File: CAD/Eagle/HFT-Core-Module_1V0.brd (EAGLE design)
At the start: 96.5 x 96.5 mm, 333 parts, among them Q0521 ABS07-32.768KHZ, Q0811 ABM03B-32.000MHZ, Q0911 ABM3B-16MHZ-10-R50-1-U, T1101 MMBT2222, T1102 MMBT2222, T1103 MMBT2222, U0111 STM32L4Z_144PIN_SMPS, U0431 PAM2305AAB120, U0601 LM4120IM5-3.0, U0611 MAX5217, U0631 CFPT-141-20MHZ, U0641 OPA354, U0701 Si5338, U0801 SX1276, U0901 AX5243, U1001 MCP3911A0-E-SS, U1011 MAX5136AGTG+, U1021 OPA354, U1031 OPA354, U1041 OPA354, U1101 NHD-C0220BIZ_2X20CHARS, U1201 MPU-9250, U1211 MS5607-02BA03, U1221 SHT31-DIS, U1301 SOLARPANEL_3V3_5MA1_25MM_X_20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, U1302 SPV1040T, U1401 TS5A23166, U1501 PAM2305AAB330, U1601 TS5A23166, U1701 TS5A23166, U1801 TS5A23166, X1161 TTE_EN11-HSM, X2001 SMA_SMT_AMPHENOL-901-143, X2011 SMA_SMT_AMPHENOL-901-143, X2101 CUI SJ1-3535NS, X2111 CUI SJ1-3535NS, X2211 2X20/90_1MM27_HARWIN_M50-3202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, X2212 2X20/90_1MM27_HARWIN_M50-3202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, X2221 2X20/90_1MM27_HARWIN_M50-3202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, X2222 2X20/90_1MM27_HARWIN_M50-3202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, X2231 2X20/90_1MM27_HARWIN_M50-3202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, X2232 2X20/90_1MM27_HARWIN_M50-3202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

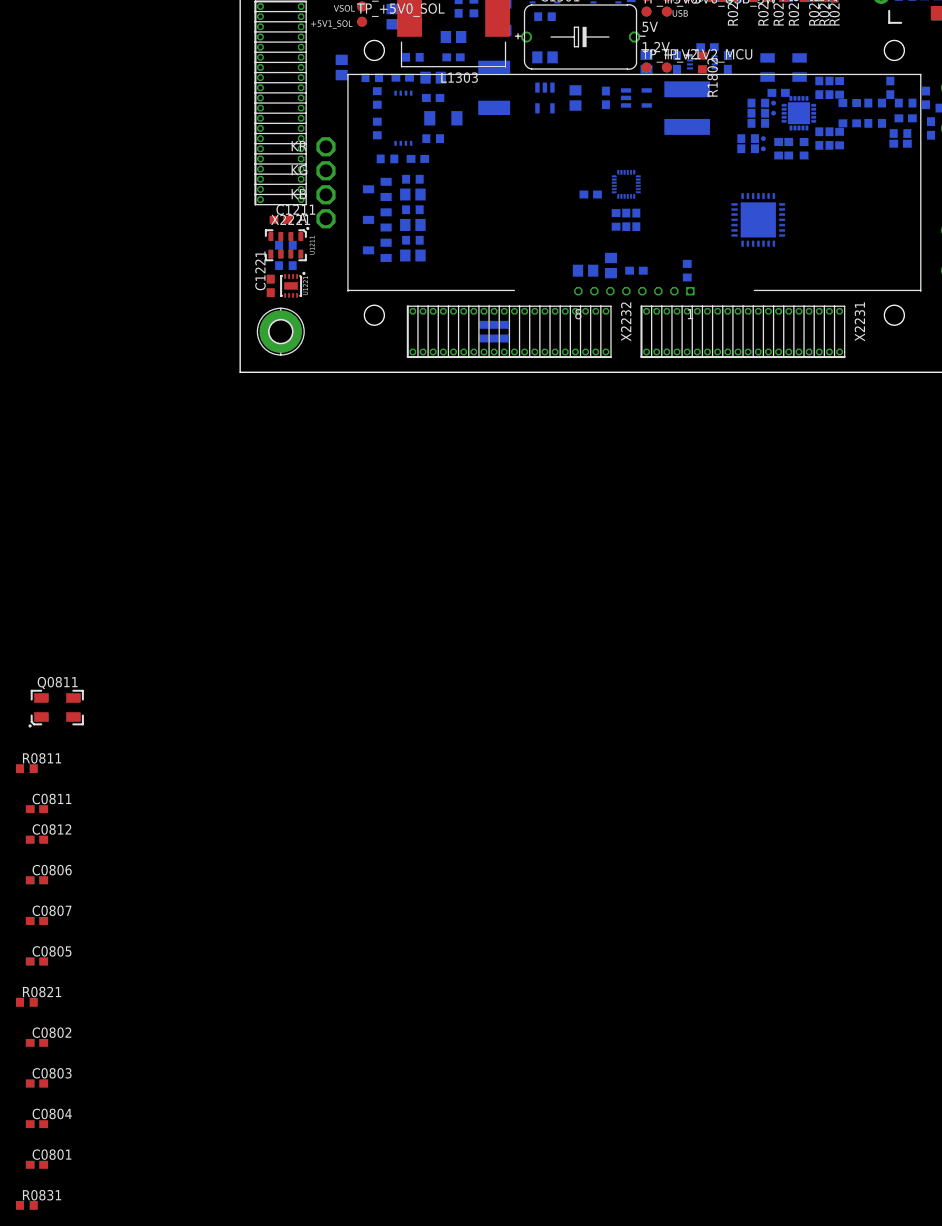
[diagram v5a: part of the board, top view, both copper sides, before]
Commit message: HW_1V0_trySX - some of the SX chip components placed
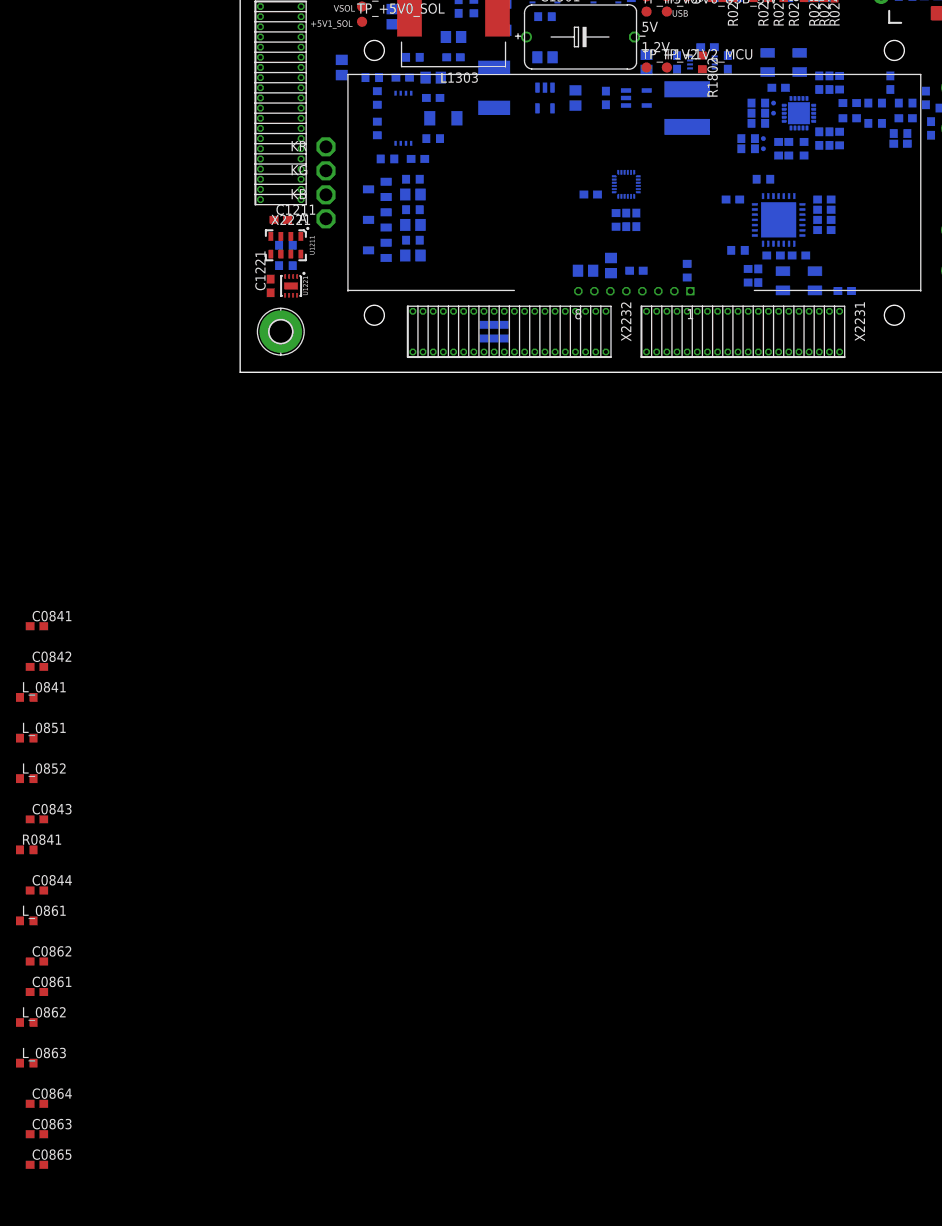
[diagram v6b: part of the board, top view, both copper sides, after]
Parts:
- added C0841, C0842, C0843, C0844, C0861, C0862, C0863, C0864, C0865: (no value), rcl:C0603
- added L_0841, L_0851, L_0852, L_0861, L_0862, L_0863: (no value), rcl:R0603
- added R0841: 0R, rcl:R0603
- moved R0831 157.9 mm to (65.4, 24.1), flipped to the bottom, turned to 180 degrees
- moved C0801 155.7 mm to (73.0, 21.6), flipped to the bottom, turned to 180 degrees
- moved C0803 145.1 mm to (73.0, 17.8), flipped to the bottom
- moved C0804 144.7 mm to (61.6, 21.6), flipped to the bottom, turned to 180 degrees
- moved C0802 143.3 mm to (73.0, 20.3), flipped to the bottom
- moved C0805 135.2 mm to (73.0, 19.1), flipped to the bottom
- moved R0821 129.4 mm to (62.2, 15.2), flipped to the bottom, turned to 180 degrees
- moved C0807 124.1 mm to (66.7, 14.6), flipped to the bottom, turned to 180 degrees
- moved C0806 123.2 mm to (69.8, 14.6), flipped to the bottom
- moved C0812 122.1 mm to (75.6, 10.2), flipped to the bottom
- moved C0811 112.1 mm to (64.8, 12.1), flipped to the bottom, turned to 270 degrees
- moved R0811 109.2 mm to (63.5, 12.1), flipped to the bottom, turned to 270 degrees
- moved Q0811 107.0 mm to (69.8, 11.4), flipped to the bottom, turned to 180 degrees
- moved U0801 2.54 mm to (67.3, 19.1), turned to 90 degrees
- moved C0901 0.64 mm to (67.3, 35.6)
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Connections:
- net XTB_R renamed SX_XTB_R
- new net N$1: C0844.2
- new net SX_PA_BOOST: L_0851.1, U0801.27
- new net SX_PA_BOOST_2: L_0851.2, L_0852.1
- new net SX_RFI_HF: C0841.1, L_0841.1, U0801.21
- new net SX_RFI_HF_2: C0842.1, C0843.1, L_0841.2
- new net SX_RFI_HF_3: C0843.2, R0841.1
- new net SX_RFI_HF_4: C0844.1, R0841.2
- new net SX_RFO_HF: C0861.1, C0862.1, L_0861.1, U0801.22
- new net SX_RFO_HF_2: C0862.2, L_0862.1
- new net SX_RFO_HF_3: C0863.1, C0864.1, L_0862.2, L_0863.1
- new net SX_RFO_HF_4: C0864.2, C0865.1, L_0863.2
- net GND: now also C0841.2, C0842.2, C0861.2, C0863.2, C0865.2
- net SX_VR_PA: now also L_0852.2, L_0861.2

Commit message: HW_1V0_trySX - RF front end added
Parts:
- removed C0842: (no value), rcl:C0603
- removed L_0851: (no value), rcl:R0603
- removed R0922: 47R, rcl:R0603
- added C0846, C0873, C0975: 47pF, rcl:C0603
- added C0850, C0858, C0872: 0pF, rcl:C0603
- added C0851, C0852: (no value), rcl:C0603
- added C0853, C0871: 4.7pF, rcl:C0603
- added C0856, C0859: 6.8pF, rcl:C0603
- added C0857: 2.7pF, rcl:C0603
- added L0854: 15nH, rcl:R0603
- added L0856, L0858, R0874: 0R, rcl:R0603
- added L0857: 12nH, rcl:R0603
- added L0871: 18nH, rcl:R0603
- added R0801: 100R, rcl:R0603
- added R0802, R0803, R0804, R0805, R0806, R0807: 47R, rcl:R0603
- C0841: value (none) -> 0pF
- C0843: value (none) -> 3.3pF
- C0844: value (none) -> 47pF
- C0861: value (none) -> 1.5pF
- C0862: value (none) -> 33pF
- C0863: value (none) -> 4.7pF
- C0864: value (none) -> 1.2pF
- C0865: value (none) -> 1.8pF
- L0842, L0862: value (none) -> 10nH
- L0851: value (none) -> 68nH
- L0861: value (none) -> 33nH
- L0864: value (none) -> 6.2nH
- moved C0843 19.1 mm to (-25.4, -36.8)
- moved C0844 8.89 mm to (-25.4, -55.9)
- renumbered L_0841 to L0842, L_0852 to L0851, L_0861 to L0861, L_0862 to L0862, L_0863 to L0864, R0841 to R0845
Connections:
- removed net AX1_SYSCLK_R: R0922.2
- removed net N$1: C0844.2
- removed net SX_PA_BOOST: L_0851.1, U0801.27
- removed net SX_PA_BOOST_2: L0851.1, L_0851.2
- new net SX_DIO0: R0802.1, U0801.8
- new net SX_DIO0_2: R0802.2
- new net SX_DIO1: R0803.1, U0801.9
- new net SX_DIO1_2: R0803.2
- new net SX_DIO2: R0804.1, U0801.10
- new net SX_DIO2_2: R0804.2
- new net SX_DIO3: R0805.1, U0801.11
- new net SX_DIO3_2: R0805.2
- new net SX_DIO4: R0806.1, U0801.12
- new net SX_DIO4_2: R0806.2
- new net SX_DIO5: R0807.1, U0801.13
- new net SX_DIO5_2: R0807.2
- new net SX_RFI_HF_5: C0846.2
- new net SX_RFI_LF: C0871.1, L0871.1, U0801.1
- new net SX_RFI_LF_2: C0871.2, C0872.2, C0873.1
- new net SX_RFI_LF_3: C0873.2, R0874.1
- new net SX_RFI_LF_4: C0975.1, R0874.2
- new net SX_RFI_LF_5: C0975.2
- new net SX_RFO_LF: C0853.1, L0851.1, L0854.1, U0801.28
- new net SX_RFO_LF_2: L0854.2, L0856.1
- new net SX_RFO_LF_3: C0856.1, C0857.1, L0856.2, L0857.1
- new net SX_RFO_LF_4: C0857.2, C0858.1, C0859.1, L0857.2, L0858.1
- new net SX_RFO_LF_5: C0850.1, C0858.2, L0858.2
- new net SX_RXTX: R0801.1, U0801.20
- new net SX_RXTX_2: R0801.2
- net AX1_SYSCLK: no longer R0922.1
- net GND: now also C0843.2, C0850.2, C0851.2, C0852.2, C0853.2, C0856.2, C0859.2, C0872.1, L0871.2; no longer C0842.2
- net SX_RFI_HF_2: now also C0844.1; no longer C0842.1
- net SX_RFI_HF_3: now also C0844.2; no longer C0843.2
- net SX_RFI_HF_4: now also C0846.1; no longer C0844.1
- net SX_VR_PA: now also C0851.1, C0852.1

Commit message: HW_1V0_trySX - renaming of nets to match with the MCU
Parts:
- R0723: value none -> 47R
- R0804, R0805, R0806, R0807: value 47R -> NC
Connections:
- net AX1_16MHZ renamed AX_16MHZ
- net AX1_SYSCLK renamed AX_SYSCLK
- net MCU_20MHZ_EN renamed MCU_OUT_20MHZ_EN
- net MCU_AX1_GPO1 renamed AX_GPIO1
- net MCU_AX1_IRQ renamed AX_IRQ
- net MCU_HICUR_EN renamed MCU_OUT_HICUR_EN
- net MCU_LCD_!RST renamed MCU_OUT_LCD_NRST
- net MCU_SPI3_AUDIO_ADC_!RESET renamed MCU_OUT_AUDIO_ADC_NRESET
- net MCU_SPI3_AUDIO_ADC_SEL renamed MCU_OUT_AUDIO_ADC_SEL
- net MCU_SPI3_AUDIO_DAC_SEL renamed MCU_OUT_AUDIO_DAC_SEL
- net MCU_SPI3_AX1_SEL renamed MCU_OUT_AX_SEL
- net MCU_SPI3_SX_SEL renamed MCU_OUT_SX_SEL
- net MCU_VDD12_EN renamed MCU_OUT_VDD12_EN
- net MCU_VUSB_EN renamed MCU_OUT_VUSB_EN
- net PC14_OSC32_IN renamed PC14_MCU_OSC32_IN
- net PC15_OSC32_OUT renamed PC15_MCU_OSC32_OUT
- net SX_!RESET_R renamed SX_NRESET
- removed net AX1_ANT: C_AX1_A3.1, C_AX1_F2.2, L_AX1_F1.2, X2001.1
- removed net AX2_ANT: X2011.1
- removed net CLK3B: R0723.1
- removed net PH0_OSC_IN: R0724.1, U0111.23, U1001.12
- removed net SX_!RESET: R0821.1
- removed net SX_DIO0_2: R0802.2
- removed net SX_DIO1_2: R0803.2
- new net CH1_ANT: X2001.1
- new net CH2_ANT: C_AX1_A3.1, C_AX1_F2.2, L_AX1_F1.2, X2011.1
- new net PH0: R0724.1, U0111.23
- new net SI5338_CLK3B_2: R0723.1, U1001.12
- net PD8: now also R0821.1
- net PG2: now also R0802.2
- net PG3: now also R0803.2
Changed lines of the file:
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@@
 <element name="R0731" library="rcl" package="R0603" value="47R" x="73.025" y="85.09"/>
 <element name="R0724" library="rcl" package="R0603" value="47R" x="73.025" y="83.82" rot="R180"/>
-<element name="R0723" library="rcl" package="R0603" value="none" x="73.025" y="82.55" rot="R180"/>
+<element name="R0723" library="rcl" package="R0603" value="47R" x="73.025" y="82.55" rot="R180"/>
 <element name="R0743" library="rcl" package="R0603" value="47R" x="64.135" y="83.82" rot="R180"/>
 <element name="R0744" library="rcl" package="R0603" value="47R" x="64.135" y="82.55" rot="R180"/>
@@
 <element name="R0801" library="rcl" package="R0603" value="100R" x="-26.67" y="-189.23"/>
 <element name="R0803" library="rcl" package="R0603" value="47R" x="-26.67" y="-194.31"/>
-<element name="R0805" library="rcl" package="R0603" value="47R" x="-26.67" y="-199.39"/>
-<element name="R0807" library="rcl" package="R0603" value="47R" x="-26.67" y="-204.47"/>
+<element name="R0805" library="rcl" package="R0603" value="NC" x="-26.67" y="-199.39"/>
+<element name="R0807" library="rcl" package="R0603" value="NC" x="-26.67" y="-204.47"/>
 <element name="R0802" library="rcl" package="R0603" value="47R" x="-26.67" y="-209.55"/>
-<element name="R0804" library="rcl" package="R0603" value="47R" x="-26.67" y="-214.63"/>
-<element name="R0806" library="rcl" package="R0603" value="47R" x="-26.67" y="-219.71"/>
+<element name="R0804" library="rcl" package="R0603" value="NC" x="-26.67" y="-214.63"/>
+<element name="R0806" library="rcl" package="R0603" value="NC" x="-26.67" y="-219.71"/>
 </elements>
 <signals>
@@
 <wire x1="45.085" y1="58" x2="46.99" y2="58" width="0" layer="19" extent="1-1"/>
 </signal>
-<signal name="PH0_OSC_IN">
+<signal name="PH0">
 <contactref element="U0111" pad="23"/>
 <contactref element="R0724" pad="1"/>
-<contactref element="U1001" pad="12"/>
-<wire x1="75.505" y1="83.32" x2="73.875" y2="83.82" width="0" layer="19" extent="1-16"/>
 <wire x1="55.415" y1="60.43" x2="73.875" y2="83.82" width="0" layer="19" extent="1-1"/>
 </signal>
-<signal name="PC15_OSC32_OUT">
+<signal name="PC15_MCU_OSC32_OUT">
 <contactref element="U0111" pad="9"/>
 <contactref element="Q0521" pad="1"/>
@@
 <wire x1="49.11" y1="71.12" x2="49.55" y2="68.58" width="0" layer="19" extent="1-1"/>
 </signal>
-<signal name="PC14_OSC32_IN">
+<signal name="PC14_MCU_OSC32_IN">
 <contactref element="U0111" pad="8"/>
 <contactref element="Q0521" pad="2"/>
@@
 <signal name="PG3">
 <contactref element="U0111" pad="88"/>
+<contactref element="R0803" pad="2"/>
+<wire x1="76.665" y1="61.505" x2="-25.82" y2="-194.31" width="0" layer="19" extent="1-1"/>
 </signal>
 <signal name="PG2">
 <contactref element="U0111" pad="87"/>
+<contactref element="R0802" pad="2"/>
+<wire x1="76.665" y1="61.005" x2="-25.82" y2="-209.55" width="0" layer="19" extent="1-1"/>
 </signal>
 <signal name="PD7">
@@
 <signal name="PD8">
 <contactref element="U0111" pad="77"/>
+<contactref element="R0821" pad="1"/>
+<wire x1="61.38" y1="15.24" x2="76.665" y2="56.005" width="0" layer="19" extent="1-16"/>
 </signal>
 <signal name="PC12">
@@
 <wire x1="55.88" y1="46.99" x2="47.27" y2="47.24" width="0" layer="19" extent="1-16"/>
 </signal>
-<signal name="MCU_20MHZ_EN">
+<signal name="MCU_OUT_20MHZ_EN">
 <contactref element="U0601" pad="3"/>
 <contactref element="U1701" pad="3"/>
@@
 <signal name="P$8">
 </signal>
-<signal name="MCU_VUSB_EN">
+<signal name="MCU_OUT_VUSB_EN">
 <contactref element="U1401" pad="3"/>
 <contactref element="U1401" pad="7"/>
@@
 <wire x1="36.55" y1="46.74" x2="39.65" y2="47.24" width="0" layer="19" extent="16-16"/>
 </signal>
-<signal name="MCU_HICUR_EN">
+<signal name="MCU_OUT_HICUR_EN">
 <contactref element="U1601" pad="3"/>
 <contactref element="U1601" pad="7"/>
@@
 <wire x1="64.985" y1="82.55" x2="66.63" y2="82.935" width="0" layer="19" extent="1-1"/>
 </signal>
-<signal name="CLK3B">
+<signal name="SI5338_CLK3B_2">
 <contactref element="R0723" pad="1"/>
+<contactref element="U1001" pad="12"/>
+<wire x1="75.505" y1="83.32" x2="73.875" y2="82.55" width="0" layer="19" extent="1-16"/>
 </signal>
 <signal name="SI5338_IN_CLK1">
@@
 <wire x1="70.485" y1="28.79" x2="70.35" y2="30.535" width="0" layer="19" extent="16-16"/>
 </signal>
-<signal name="AX1_SYSCLK">
+<signal name="AX_SYSCLK">
 <contactref element="U0901" pad="9"/>
 <contactref element="R0921" pad="1"/>
 <wire x1="67.31" y1="28.79" x2="69.35" y2="30.535" width="0" layer="19" extent="16-16"/>
 </signal>
-<signal name="AX1_16MHZ">
+<signal name="AX_16MHZ">
 <contactref element="R0921" pad="2"/>
 <contactref element="R0714" pad="1"/>
 <wire x1="67.31" y1="27.09" x2="69.215" y2="77.89" width="0" layer="19" extent="1-16"/>
 </signal>
-<signal name="MCU_AX1_IRQ">
+<signal name="AX_IRQ">
 <contactref element="U0901" pad="14"/>
 <contactref element="R0951" pad="2"/>
@@
 <wire x1="65.62" y1="31.115" x2="68" y2="31.885" width="0" layer="19" extent="16-16"/>
 </signal>
-<signal name="MCU_AX1_GPO1">
+<signal name="AX_GPIO1">
 <contactref element="R0961" pad="2"/>
 <contactref element="U0901" pad="15"/>
@@
 <wire x1="86.36" y1="31.33" x2="87.415" y2="33.02" width="0" layer="19" extent="16-16"/>
 </signal>
-<signal name="AX1_ANT">
+<signal name="CH2_ANT">
 <contactref element="L_AX1_F1" pad="2"/>
 <contactref element="C_AX1_F2" pad="2"/>
 <contactref element="C_AX1_A3" pad="1"/>
-<contactref element="X2001" pad="1"/>
-<wire x1="89.115" y1="33.02" x2="91.44" y2="33.02" width="0" layer="19" extent="16-16"/>
-<wire x1="91.44" y1="30.695" x2="91.44" y2="33.02" width="0" layer="19" extent="16-16"/>
-<wire x1="85.725" y1="35.14" x2="89.115" y2="33.02" width="0" layer="19" extent="16-16"/>
-</signal>
-<signal name="AX2_ANT">
 <contactref element="X2011" pad="1"/>
+<wire x1="91.44" y1="30.695" x2="89.115" y2="33.02" width="0" layer="19" extent="16-16"/>
+<wire x1="85.725" y1="35.14" x2="89.115" y2="33.02" width="0" layer="19" extent="16-16"/>
+<wire x1="91.44" y1="15.24" x2="91.44" y2="30.695" width="0" layer="19" extent="16-16"/>
 </signal>
 <signal name="LCD_C1+">
@@
 <wire x1="67.31" y1="22.025" x2="68" y2="32.385" width="0" layer="19" extent="16-16"/>
 </signal>
-<signal name="MCU_SPI3_AX1_SEL">
+<signal name="MCU_OUT_AX_SEL">
 <contactref element="R0253" pad="2"/>
 <contactref element="U0901" pad="10"/>
@@
 <wire x1="50.8254" y1="35.2298" x2="50.8" y2="37.785" width="0" layer="19" extent="16-16"/>
 </signal>
-<signal name="MCU_VDD12_EN">
+<signal name="MCU_OUT_VDD12_EN">
 <contactref element="U1801" pad="3"/>
 <contactref element="U1801" pad="7"/>
@@
 <wire x1="50.8254" y1="33.3502" x2="55.88" y2="30.67" width="0" layer="19" extent="16-16"/>
 </signal>
-<signal name="MCU_LCD_!RST">
+<signal name="MCU_OUT_LCD_NRST">
 <contactref element="R0272" pad="2"/>
 <contactref element="U1101" pad="1"/>
@@
 <wire x1="86.78" y1="66.04" x2="83.2104" y2="71.4248" width="0" layer="19" extent="16-16"/>
 </signal>
-<signal name="MCU_SPI3_AUDIO_ADC_!RESET">
+<signal name="MCU_OUT_AUDIO_ADC_NRESET">
 <contactref element="U1001" pad="18"/>
 <contactref element="R0261" pad="2"/>
@@
 <wire x1="73.24" y1="75.565" x2="77.47" y2="85.785" width="0" layer="19" extent="16-16"/>
 </signal>
-<signal name="MCU_SPI3_AUDIO_ADC_SEL">
+<signal name="MCU_OUT_AUDIO_ADC_SEL">
 <contactref element="U1001" pad="14"/>
 <contactref element="R0262" pad="2"/>
@@
 <wire x1="70.765" y1="73.355" x2="71.54" y2="75.565" width="0" layer="19" extent="1-16"/>
 </signal>
-<signal name="MCU_SPI3_AUDIO_DAC_SEL">
+<signal name="MCU_OUT_AUDIO_DAC_SEL">
 <contactref element="R0263" pad="2"/>
 <contactref element="U1011" pad="10"/>
@@
 <wire x1="72.175" y1="19.05" x2="70.285" y2="19.05" width="0" layer="19" extent="16-16"/>
 </signal>
-<signal name="SX_!RESET_R">
+<signal name="SX_NRESET">
 <contactref element="U0801" pad="7"/>
 <contactref element="R0821" pad="2"/>
 <wire x1="63.08" y1="15.24" x2="65.36" y2="16.075" width="0" layer="19" extent="16-16"/>
 </signal>
-<signal name="SX_!RESET">
-<contactref element="R0821" pad="1"/>
-</signal>
 <signal name="SX_MISO">
 <contactref element="U0801" pad="17"/>
@@
 <wire x1="66.66" y1="22.025" x2="66.255" y2="24.13" width="0" layer="19" extent="16-16"/>
 </signal>
-<signal name="MCU_SPI3_SX_SEL">
+<signal name="MCU_OUT_SX_SEL">
 <contactref element="U0801" pad="19"/>
 <contactref element="R0254" pad="2"/>
@@
 <wire x1="64.335" y1="20.35" x2="-27.52" y2="-204.47" width="0" layer="19" extent="1-16"/>
 </signal>
-<signal name="SX_DIO0_2">
-<contactref element="R0802" pad="2"/>
-</signal>
-<signal name="SX_DIO1_2">
-<contactref element="R0803" pad="2"/>
-</signal>
 <signal name="SX_DIO2_2">
 <contactref element="R0804" pad="2"/>
@@
 <contactref element="R0807" pad="2"/>
 </signal>
+<signal name="CH1_ANT">
+<contactref element="X2001" pad="1"/>
+</signal>
 </signals>
